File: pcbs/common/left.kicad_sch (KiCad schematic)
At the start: 89 parts, among them J2 TRS

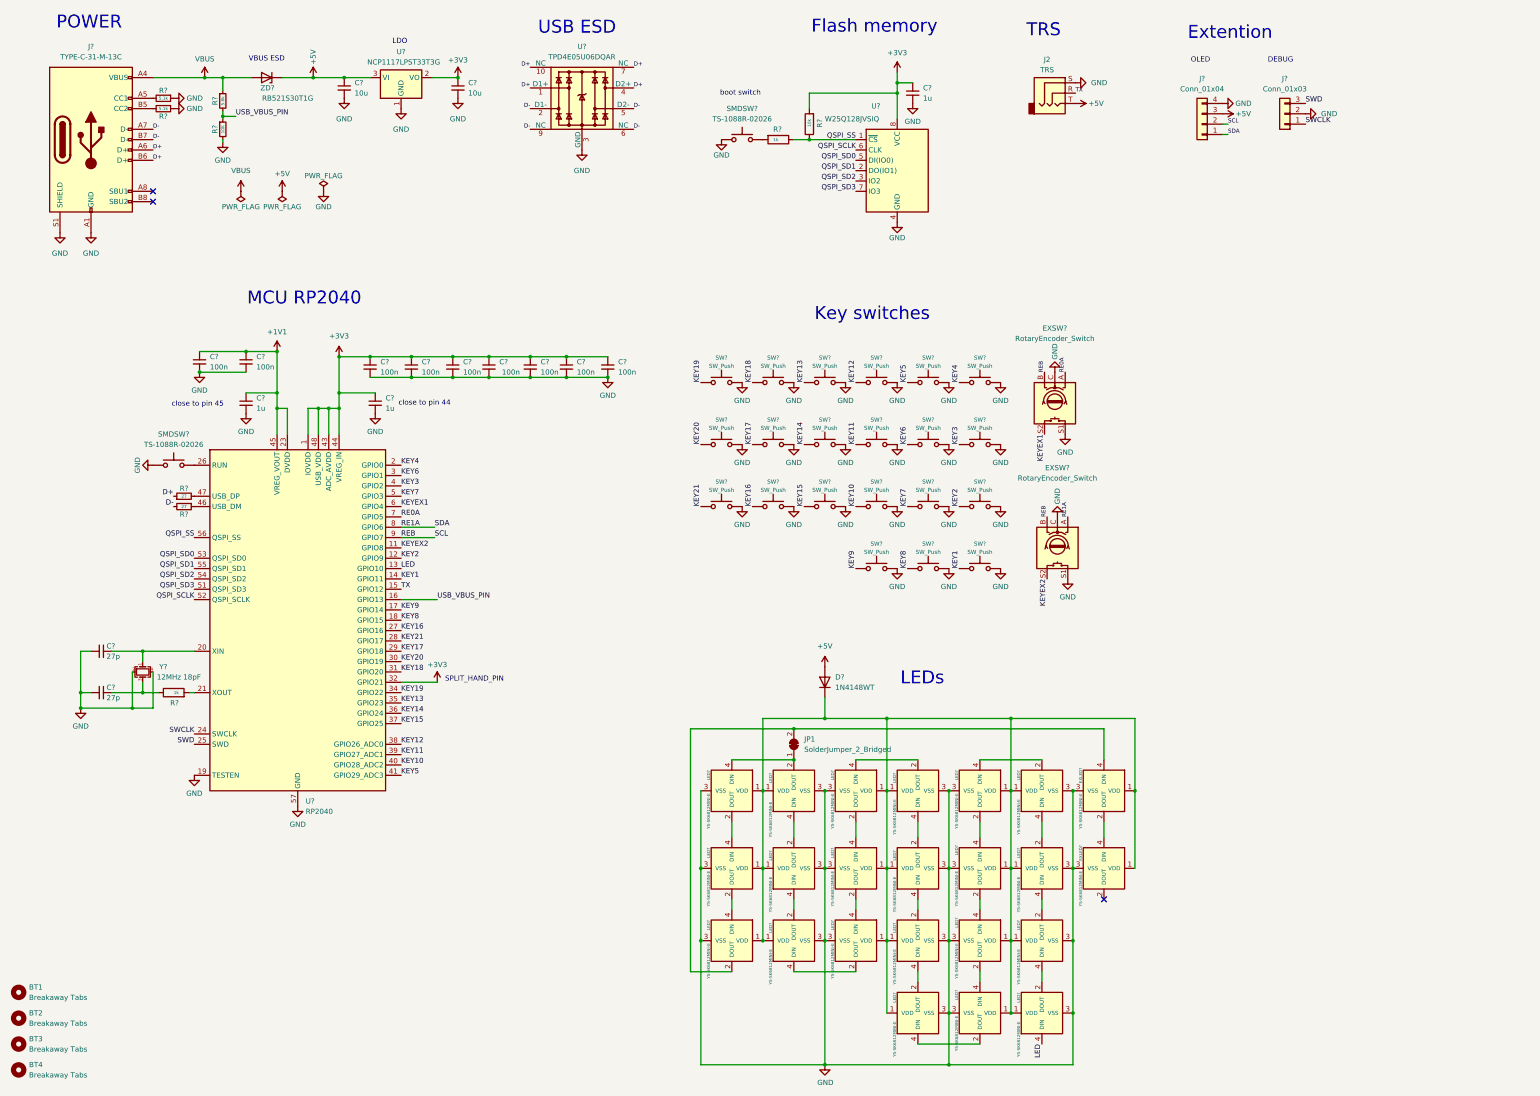
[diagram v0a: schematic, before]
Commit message: PCB re-route for EMI (cherry)
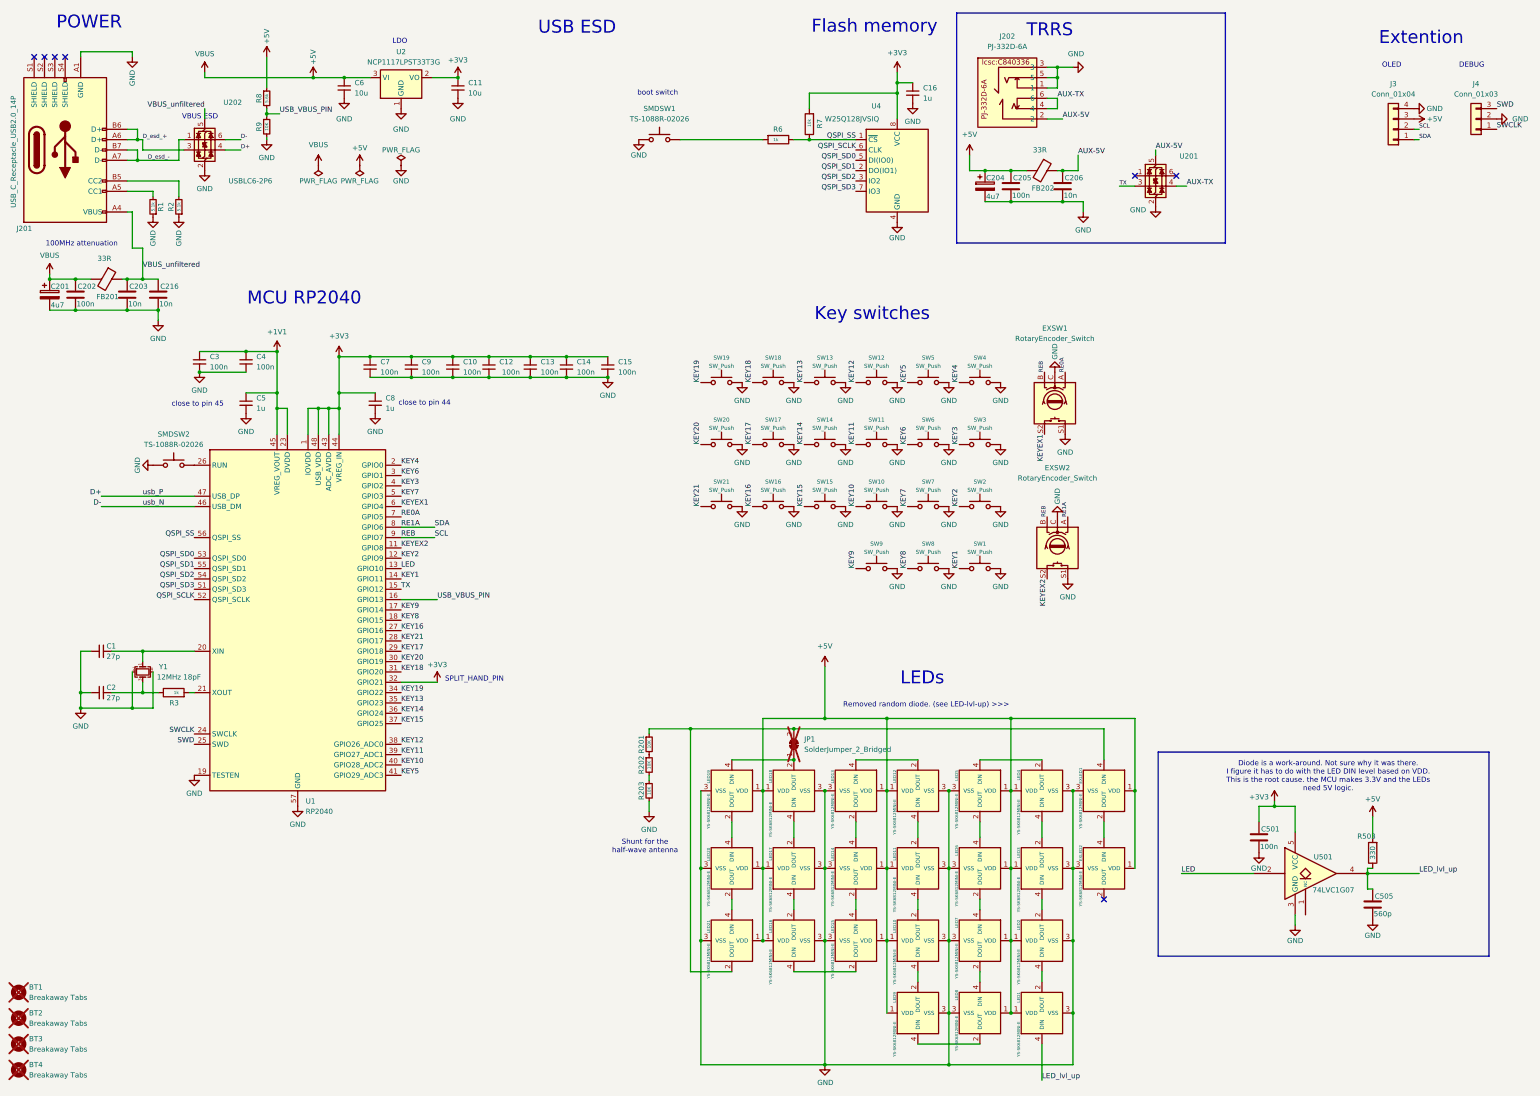
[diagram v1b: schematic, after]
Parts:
- removed D?: 1N4148WT, Diode_SMD:D_SOD-523, symbol Diode:1N4148WT
- removed J2: TRS, kbd_local:PJ-398A-5A_PJ-399B-6A, symbol Connector_Audio:AudioJack3
- removed J?: TYPE-C-31-M-13C, kbd_local:TYPE-C-31-M-13C, symbol Connector:USB_C_Receptacle_USB2.0
- removed R? (x2): 27, Resistor_SMD:R_0402_1005Metric, symbol Device:R_Small
- removed U?: TPD4E05U06DQAR, Package_SON:USON-10_2.5x1.0mm_P0.5mm, symbol Power_Protection:TPD4EUSB30
- removed ZD?: RB521S30T1G, Diode_SMD:D_SOD-523, symbol Diode:ESD5Zxx
- added C201, C204: 4u7, Capacitor_SMD:C_1210_3225Metric, symbol Device:C_Polarized
- added C202, C205, C501: 100n, Capacitor_SMD:C_0402_1005Metric, symbol Device:C
- added C203, C206, C216: 10n, Capacitor_SMD:C_0402_1005Metric, symbol Device:C
- added C505: 560p, Capacitor_SMD:C_0402_1005Metric, symbol Device:C
- added FB201, FB202: 33R, Inductor_SMD:L_1206_3216Metric, symbol Device:FerriteBead
- added J201: USB_C_Receptacle_USB2.0_14P, keyboard_ohne_emi:USB4105, symbol Connector:USB_C_Receptacle_USB2.0_14P
- added J202: PJ-332D-6A, keyboard_ohne_emi:PJ-332D-6A, symbol kbd:TRRS_1A
- added R201, R202, R203: 10K, Resistor_SMD:R_0402_1005Metric, symbol Device:R_Small
- added R503: 330, Resistor_SMD:R_0402_1005Metric, symbol Device:R
- added U201, U202: USBLC6-2P6, ESP32-S3-CaV2:USBLC6-2P6, symbol Power_Protection:USBLC6-2P6
- added U501: 74LVC1G07, Package_TO_SOT_SMD:SOT-353_SC-70-5, symbol 74xGxx:74LVC1G07
- BT1, BT2, BT3, BT4, JP1: now not fitted
- C10, C12, C13, C14, C15, C3, C4, C7, C9: renamed from C?; JLCPCB Part # (none) -> C133086; LCSC Part # (none) -> C133086
- SMDSW1, SMDSW2: renamed from SMDSW?; LCSC Part # (none) -> C455280
- U1: renamed from U?; LCSC Part # (none) -> C2040
- U2: renamed from U?; LCSC Part # (none) -> C146799
- U4: renamed from U?; LCSC Part # (none) -> C113767
- Y1: renamed from Y?; LCSC Part # (none) -> C91749
- gave numbers to parts that had none: 62
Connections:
- net VBUS is gone; now on net +5V: R8.1
- net +3V3: now also C501.1, U501.5 (VCC)
- net +5V: now also EXLED1.1 (VDD), EXLED2.1 (VDD), LED1.1 (VDD), LED10.1 (VDD), LED11.1 (VDD), LED12.1 (VDD), LED13.1 (VDD), LED14.1 (VDD), LED15.1 (VDD), LED16.1 (VDD), LED17.1 (VDD), LED18.1 (VDD), LED19.1 (VDD), LED2.1 (VDD), LED20.1 (VDD), LED21.1 (VDD), LED3.1 (VDD), LED4.1 (VDD), LED5.1 (VDD), LED6.1 (VDD), LED7.1 (VDD), LED8.1 (VDD), LED9.1 (VDD), C201.1, C202.1, C204.1, C205.1, FB201.2, FB202.2, R503.2
- net D+: now also U1.47 (USB_DP), U202.4 (I/O2)
- net D-: now also U1.46 (USB_DM), U202.6 (I/O1)
- net GND: now also C201.2, C202.2, C203.2, C204.2, C205.2, C206.2, C216.2, C501.2, C505.2, J201.A1 (GND), J201.B1 (GND), J202.1, J202.3, J202.5, R203.2, U201.2 (GND), U202.2 (GND), U501.3 (GND)
- net LED: now also U501.2; no longer LED1.4 (DIN)
- net TX: now also U201.3 (I/O2)
- net at EXLED1.4 (DIN), JP1.2 (B), LED21.2 (DOUT): now also R201.1
- net at R1.2: now also J201.A5 (CC1)
- net at R2.2: now also J201.B5 (CC2)
- new net: R201.2, R202.1
- new net: R202.2, R203.1
- new net AUX-5V: C206.1, FB202.1, J202.2, U201.5 (VBUS)
- new net AUX-TX: J202.4, J202.6, U201.4 (I/O2)
- new net D_esd_+: J201.A6 (D+), J201.B6 (D+), U202.3 (I/O2)
- new net D_esd_-: J201.A7 (D-), J201.B7 (D-), U202.1 (I/O1)
- new net LED_lvl_up: C505.1, LED1.4 (DIN), R503.1, U501.4
- new net VBUS_unfiltered: C203.1, C216.1, FB201.1, J201.A4 (VBUS), J201.B4 (VBUS), U202.5 (VBUS)
- no-connect marks 3 -> 7
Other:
- note added: "100MHz attenuation"
- note added: "Diode is a work-around. Not sure why it was there. I figure it has to do with the LED DIN level based on VDD. This is the root cause. the MCU makes 3.3V and the LEDs need 5V logic."
- note added: "Removed random diode. (see LED-lvl-up) >>>"
- note added: "Shunt for the half-wave antenna"
- note added: "TRRS"
- note removed: "TRS"
- moved on the sheet: J3, J4, R1, R2, R8, R9, SMDSW1
